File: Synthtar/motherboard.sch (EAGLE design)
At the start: 21 parts

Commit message: joystick breakout for whammy
created joystick breakout and added some more headers/notes to the mainboard
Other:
- note added: "16 buttons - 4 body 4 quick 4 menu 4 additional (2 used)"
- note added: "HCT version of the shift register will take 3.3v fine, HC version will not and will require a level shifter"
- note added: "at that point i might as well onboard the nano's shifter and only use a 4 pin over there as well"
- note added: "level shifter for indicators too? just to be safe? hmm"
- note added: "make single board for all digital body inputs, 8 pins"
- note added: "needs level shifter... will only work with 3.3v"
- note added: "on board for indicators and i2c, offboard for nano/screen"
- note added: "shift on board or on other side? on board will require fewer wires, and i'm not really doing much here anyway..."
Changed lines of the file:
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@@
 make 4 pin header for i2c, onboard level shifter?
 amp on board?</text>
+<text x="-25.4" y="-30.48" size="1.778" layer="91">level shifter for indicators too? just to be safe? hmm</text>
+<text x="-25.4" y="-33.02" size="1.778" layer="91">at that point i might as well onboard the nano's shifter and only use a 4 pin over there as well</text>
+<text x="-25.4" y="-40.64" size="1.778" layer="91">HCT version of the shift register will take 3.3v fine, HC version will not and will require a level shifter</text>
+<text x="-25.4" y="-45.72" size="1.778" layer="91">shift on board or on other side? on board will require fewer wires, and i'm not really doing much here anyway...</text>
+<text x="-78.74" y="86.36" size="1.778" layer="91">needs level shifter... will only work with 3.3v</text>
+<text x="-25.4" y="-50.8" size="1.778" layer="91">on board for indicators and i2c, offboard for nano/screen</text>
+<text x="-25.4" y="-55.88" size="1.778" layer="91">make single board for all digital body inputs, 8 pins</text>
+<text x="-25.4" y="-71.12" size="1.778" layer="91">16 buttons -
+4 body
+4 quick
+4 menu
+4 additional (2 used)</text>
 </plain>
 <instances>

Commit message: big changes
changed a ton
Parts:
- removed ADDITIONAL_HEADER, BODY_HEADER, MENU_HEADER, QUIK_HEADER: 5-PIN-HEADER, mask_lbr:5-PIN-HEADER
- removed U$1, U$2, U$3, U$4, U$6, U$9: 3-PIN-HEADER, mask_lbr:3-PIN-HEADER
- removed VS1: VS1053B, synthtar:VS1053B
- added U$10: 8-PIN-HEADER, mask_lbr:8-PIN-HEADER
- added U$11, U$13: 4-PIN-HEADER, mask_lbr:4-PIN-HEADER
- added U$12: LEVEL-SHIFTER, mask_lbr:LEVEL-SHIFTER
- added U$14: 3-PIN-HEADER, mask_lbr:3-PIN-HEADER
- added X1: (no value), mask_lbr:W237-102
- U$7: value 5-PIN-HEADER -> 2-PIN-HEADER; device mask_lbr:5-PIN-HEADER -> mask_lbr:2-PIN-HEADER
- U$8: value 3-PIN-HEADER -> 7-PIN-HEADER; device mask_lbr:3-PIN-HEADER -> mask_lbr:7-PIN-HEADER
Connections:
- removed net N$1: U$1.P$1, U$2.P$1, U$3.P$1, U$4.P$1, U$6.P$1
- removed net N$2: U$1.P$2, U$2.P$2, U$3.P$2, U$4.P$2, U$6.P$2
- removed net N$22: VS1.1, VS1.3V3
- removed net N$25: U$8.P$2, U$9.P$2, VS1.LOUT
- removed net N$26: U$8.P$1, U$9.P$1, VS1.ROUT
- removed net N$32: U$8.P$3, U$9.P$3, VS1.AGND1
- removed net SR_CLK: U$5.19/A5/T/SCL
- removed net SR_DATA: U$5.21/A7
- new net ANALOG_ACTIVE: U$5.19/A5/T/SCL, U$8.P$1
- new net N$3: U$12.LV2, U$7.P$1
- new net N$4: U$11.P$3, U$12.HV1
- new net N$5: U$11.P$4, U$12.HV2
- net +5V: now also U$11.P$1, U$12.HV, U$13.P$1, U$14.P$1, X1-2.KL; no longer U$7.P$1, VS1.VCC
- net ADD_BTNS: now also U$10.P$4; no longer ADDITIONAL_HEADER.P$1
- net A_IN2: now also U$8.P$4; no longer U$2.P$3
- net A_IN3: now also U$8.P$5; no longer U$3.P$3
- net A_IN4: now also U$8.P$6; no longer U$4.P$3
- net A_WHAM: now also U$8.P$7; no longer U$6.P$3
- net BODY_BTNS: now also U$10.P$1; no longer BODY_HEADER.P$1
- net B_ROW_1: now also U$10.P$5; no longer ADDITIONAL_HEADER.P$2, BODY_HEADER.P$2, MENU_HEADER.P$2, QUIK_HEADER.P$2
- net B_ROW_2: now also U$10.P$6; no longer ADDITIONAL_HEADER.P$3, BODY_HEADER.P$3, MENU_HEADER.P$3, QUIK_HEADER.P$3
- net B_ROW_3: now also U$10.P$7; no longer ADDITIONAL_HEADER.P$4, BODY_HEADER.P$4, MENU_HEADER.P$4, QUIK_HEADER.P$4
- net B_ROW_4: now also U$10.P$8; no longer ADDITIONAL_HEADER.P$5, BODY_HEADER.P$5, MENU_HEADER.P$5, QUIK_HEADER.P$5
- net GND: now also U$11.P$2, U$12.GND, U$12.GND2, U$13.P$2, U$14.P$2, U$8.P$2, X1-1.KL; no longer U$7.P$3, VS1.0, VS1.GND
- net MENU_BTNS: now also U$10.P$2; no longer MENU_HEADER.P$1
- net QUIK_BTNS: now also U$10.P$3; no longer QUIK_HEADER.P$1
- net SCREEN_BUSYLV: now also U$7.P$2; no longer U$7.P$5
- net SCREEN_DATALV: now also U$12.LV1; no longer U$7.P$4
- net VCC: now also U$12.LV; no longer U$7.P$2
- net VOL_RD: now also U$8.P$3; no longer U$1.P$3
- net VS_MIDI: now also U$13.P$3, U$14.P$3; no longer VS1.RX
- net VS_RST: now also U$13.P$4; no longer VS1.RST
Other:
- note added: "audio header board? need a 7 pin connector..."
- note added: "can I use this pin? arduino forum says Serial.begin dedicates the pins. I'm not receiving data from the 1053b though..."
- note added: "dno't want this to float... use jumper so we don't use it in this prototype!"
- note added: "how should I remove it? jumper to make it optional?"
- note added: "not using screen busy in this version..."
- note added: "not using this i2c in this version..."
- note added: "output to "analog" board? easy enough to make, but do I have the area to mount it? Simplifies connections..."
- note added: "pick a pin I guess..."
- note added: "pull the unused parts of this shifter low?"
- note added: "so it should be fine to init it as an output after the fact?"
- note added: "switch to 19 I guess. Just in case!"
- note added: "to audio board..."
- note added: "to matrix board..."
- note added: "to midi transmitter..."
- note added: "to neck board..."
- note added: "to power board..."
- note added: "to screenslave assembly"
- note added: "trigger this with a voltage when you measure? saves power..."
- note added: "usb data is done via an adapter cable because screw soldering to pads"
- note added: "yeah, let's have an analog board. we can add it on later!"
- note removed: "may need a distribution amp here to isolate"
- note removed: "need to measure this current"
- note removed: "to amp?"
- note removed: "to headphone jack"
- note removed: "when operating alone"
- moved on the sheet: NECK_HEADER

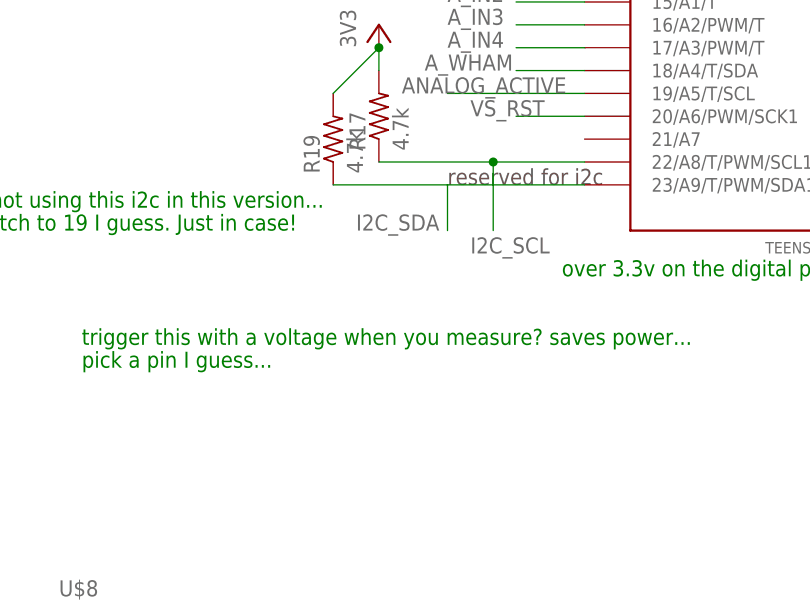
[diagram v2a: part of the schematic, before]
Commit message: changed a_active to pin 19
so it's not on a serial line. arduino forums said after Serial.begin() it becomes unpredictable
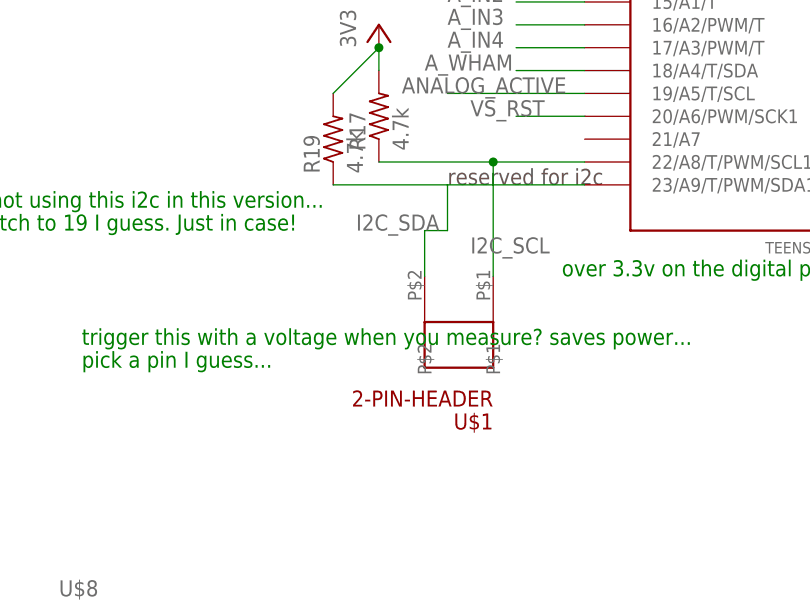
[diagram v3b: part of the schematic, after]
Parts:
- added U$1: 2-PIN-HEADER, mask_lbr:2-PIN-HEADER
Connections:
- net I2C_SCL: now also U$1.P$1
- net I2C_SDA: now also U$1.P$2
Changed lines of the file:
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@@
 <part name="U$8" library="mask_lbr" deviceset="7-PIN-HEADER" device=""/>
 <part name="SUPPLY4" library="supply2" library_urn="urn:adsk.eagle:library:372" deviceset="GND" device=""/>
+<part name="U$1" library="mask_lbr" deviceset="2-PIN-HEADER" device=""/>
 </parts>
 <sheets>
@@
 <instance part="U$8" gate="G$1" x="-99.06" y="-50.8"/>
 <instance part="SUPPLY4" gate="GND" x="-109.22" y="-63.5"/>
+<instance part="U$1" gate="G$1" x="-66.04" y="-15.24" rot="R180"/>
 </instances>
 <busses>
@@
 <pinref part="R17" gate="G$1" pin="1"/>
 <wire x1="-63.5" y1="5.08" x2="-76.2" y2="5.08" width="0.1524" layer="91"/>
-<wire x1="-63.5" y1="5.08" x2="-63.5" y2="-2.54" width="0.1524" layer="91"/>
+<wire x1="-63.5" y1="5.08" x2="-63.5" y2="-7.62" width="0.1524" layer="91"/>
 <junction x="-63.5" y="5.08"/>
 <label x="-66.04" y="-5.08" size="1.778" layer="95"/>
+<pinref part="U$1" gate="G$1" pin="P$1"/>
 </segment>
 </net>
@@
 <wire x1="-68.58" y1="2.54" x2="-68.58" y2="-2.54" width="0.1524" layer="91"/>
 <label x="-78.74" y="-2.54" size="1.778" layer="95"/>
-</segment>
-</net>
+<pinref part="U$1" gate="G$1" pin="P$2"/>
+<wire x1="-71.12" y1="-7.62" x2="-71.12" y2="-2.54" width="0.1524" layer="91"/>
+<wire x1="-71.12" y1="-2.54" x2="-68.58" y2="-2.54" width="0.1524" layer="91"/>
+</segment>
+</net>

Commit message: finished motherboard
enough jumpers to fill a bad third eye blind playlist
started making musb breakout for connecting power and data independently
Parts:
- removed R17, R19: 4.7k, rcl:R-US_0204/7
- removed U$1, U$7: 2-PIN-HEADER, mask_lbr:2-PIN-HEADER
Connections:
- removed net I2C_SCL: R17.1, U$1.P$1, U$5.22/A8/T/PWM/SCL1
- removed net I2C_SDA: R19.1, U$1.P$2, U$5.23/A9/T/PWM/SDA1
- removed net N$3: U$12.LV2, U$7.P$1
- removed net VCC: R17.2, R19.2, U$12.LV, U$5.3.3V
- new net 3VRAIL: U$12.LV, U$5.3.3V
- net SCREEN_BUSYLV: now also U$12.LV2; no longer U$7.P$2
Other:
- note added: "cutting out teensy i2c for now, re-add later when you have more time! when re-adding, use 4.7k pull-ups, and run through the level shifter to use its extra ports"
- note added: "it's on the same side anyway"
- note added: "make sure to use a 4 pin too..."
- note removed: "reserved for i2c"
